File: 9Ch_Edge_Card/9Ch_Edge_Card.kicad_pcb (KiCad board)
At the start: 2 copper layers, 39.4 x 15 mm, 1 part

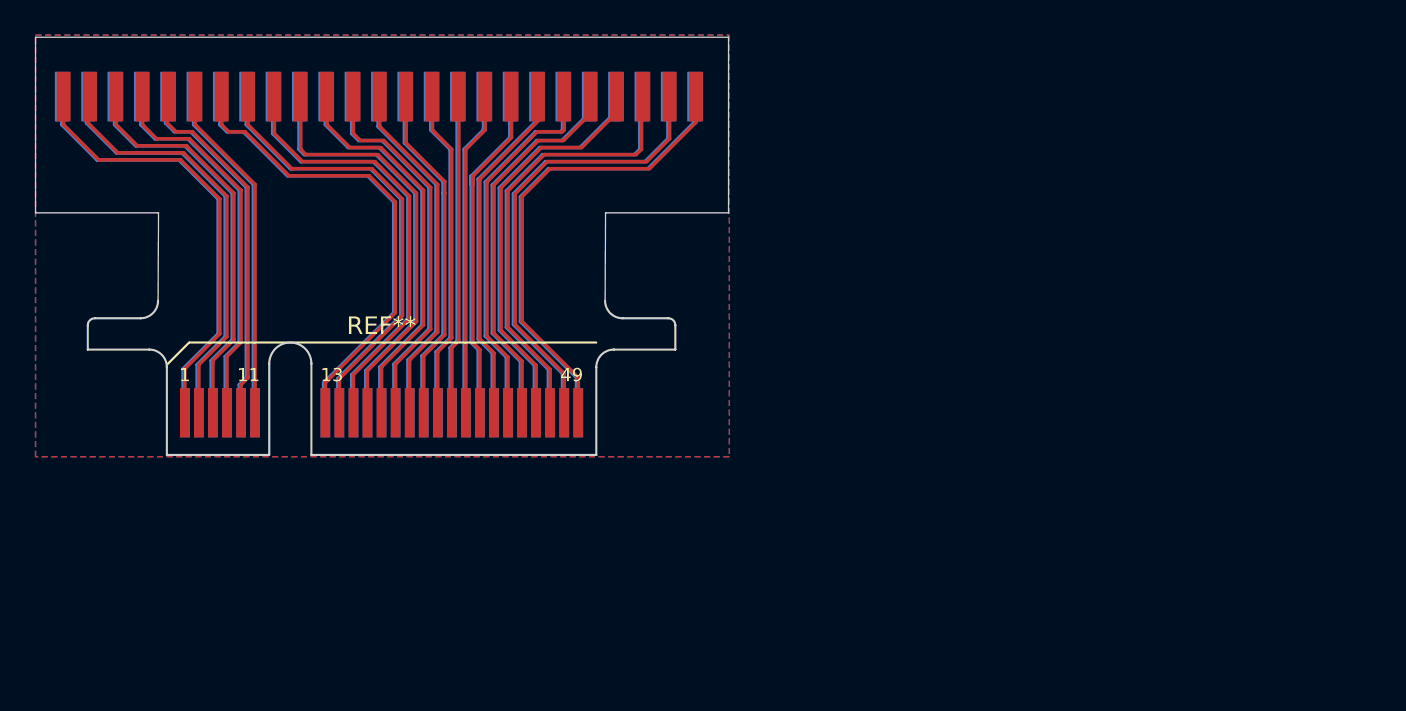
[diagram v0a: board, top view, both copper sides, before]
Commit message: Adding boards
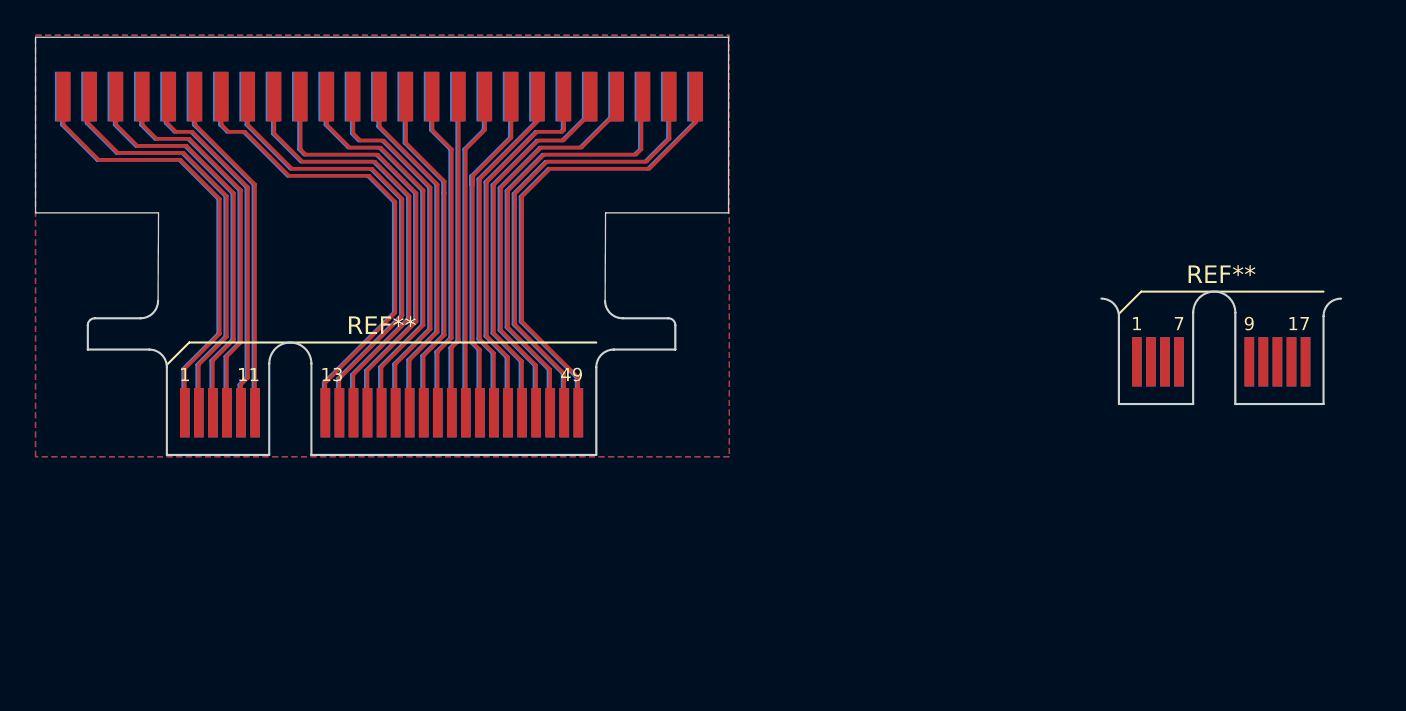
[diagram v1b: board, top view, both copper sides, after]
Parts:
- added REF**: Samtec_HSEC8-109-X-X-DV_2x09_P0.8mm_Wing_Edge, Connector_Samtec_HSEC8:Samtec_HSEC8-109-X-X-DV_2x09_P0.8mm_Wing_Edge, F.Cu at (185.0, 103.5)

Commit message: Updated boards with connector HSEC8-109-01-L-DV-A-BL
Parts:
- removed the REF** at (185.0, 103.5)
- removed the REF** at (137.2, 106.4)
- added REF**: Samtec_HSEC8-109-X-X-DV-BL_2x09_P0.8mm_Edge, Connector_Samtec_HSEC8:Samtec_HSEC8-109-X-X-DV-BL_2x09_P0.8mm_Edge, F.Cu at (182.2, 118.4)
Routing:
- net 49: track 53.5 -> 0.00 mm
- net 47: track 52.2 -> 0.00 mm
- net 45: track 50.5 -> 0.00 mm
- net 19: track 48.6 -> 0.00 mm
- net 43: track 45.8 -> 0.00 mm
- net 41: track 43.6 -> 0.00 mm
- net 23: track 42.9 -> 0.00 mm
- net 39: track 42.3 -> 0.00 mm
- net 21: track 42.3 -> 0.00 mm
- net 25: track 40.1 -> 0.00 mm
- net 37: track 39.4 -> 0.00 mm
- net 35: track 39.2 -> 0.00 mm
- net 29: track 37.6 -> 0.00 mm
- net 33: track 36.9 -> 0.00 mm
- net 27: track 36.9 -> 0.00 mm
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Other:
- board size 39.4 x 15 mm -> 20.7 x 8.8 mm
- board text added: "HSEC8-109-01-L-DV-A-BL"
